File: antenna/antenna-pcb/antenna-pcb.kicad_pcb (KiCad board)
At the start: 2 copper layers, 97 x 97 mm, 11 parts, among them J1 SMA Connector Male, U1 HHM1589D1

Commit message: bottom adapter plate sanity commit
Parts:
- added Burn1: Burn, TestPoint:TestPoint_THTPad_2.0x2.0mm_Drill1.0mm, F.Cu at (146.0, 95.0)
- added Burn2: Burn, TestPoint:TestPoint_THTPad_2.0x2.0mm_Drill1.0mm, F.Cu at (142.0, 95.0)
- added Burn3: Burn, TestPoint:TestPoint_THTPad_2.0x2.0mm_Drill1.0mm, F.Cu at (150.0, 95.0)
- added Burn4: Burn, TestPoint:TestPoint_THTPad_2.0x2.0mm_Drill1.0mm, F.Cu at (154.0, 95.0)
- added GND1: GND, TestPoint:TestPoint_THTPad_2.0x2.0mm_Drill1.0mm, F.Cu at (150.0, 100.0)
- added GND2: GND, TestPoint:TestPoint_THTPad_2.0x2.0mm_Drill1.0mm, F.Cu at (146.0, 100.0)
- added GND3: GND, TestPoint:TestPoint_THTPad_2.0x2.0mm_Drill1.0mm, F.Cu at (154.0, 100.0)
- added GND4: GND, TestPoint:TestPoint_THTPad_2.0x2.0mm_Drill1.0mm, F.Cu at (142.0, 100.0)

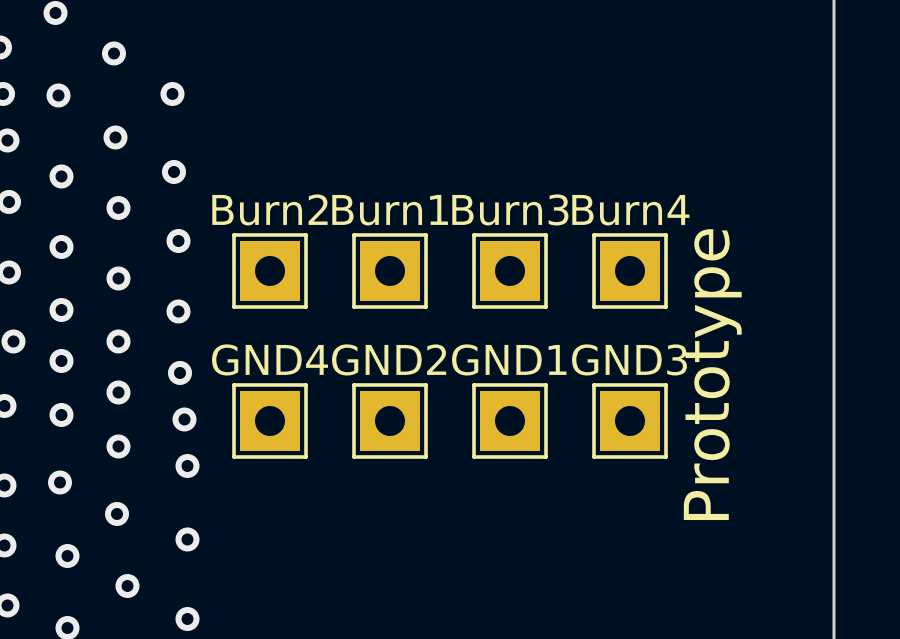
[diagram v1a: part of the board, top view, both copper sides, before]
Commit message: placed components, added traces to antenna-solar
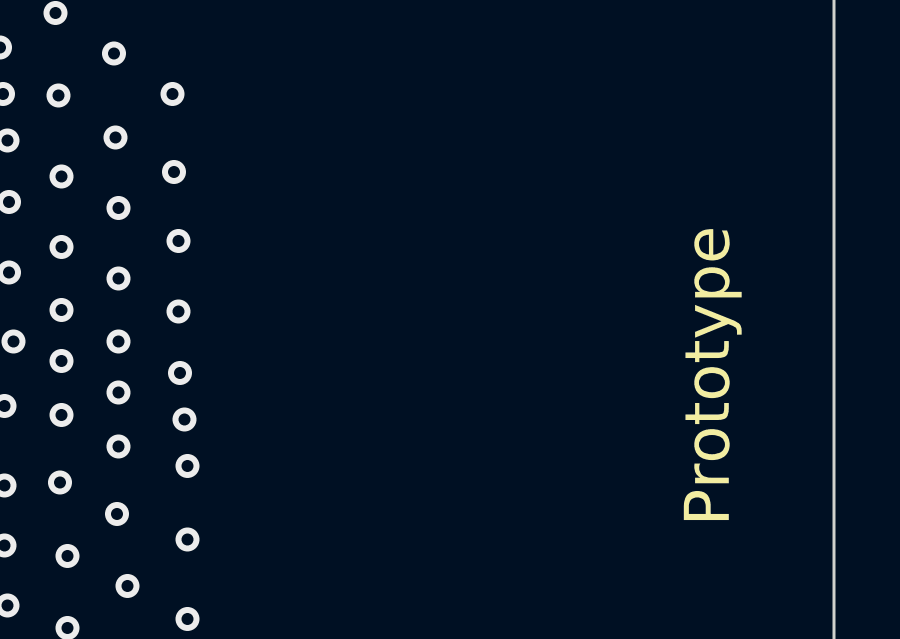
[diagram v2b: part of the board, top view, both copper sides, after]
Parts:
- removed Burn1, Burn2, Burn3, Burn4: Burn, TestPoint:TestPoint_THTPad_2.0x2.0mm_Drill1.0mm
- removed GND1, GND2, GND3, GND4: GND, TestPoint:TestPoint_THTPad_2.0x2.0mm_Drill1.0mm

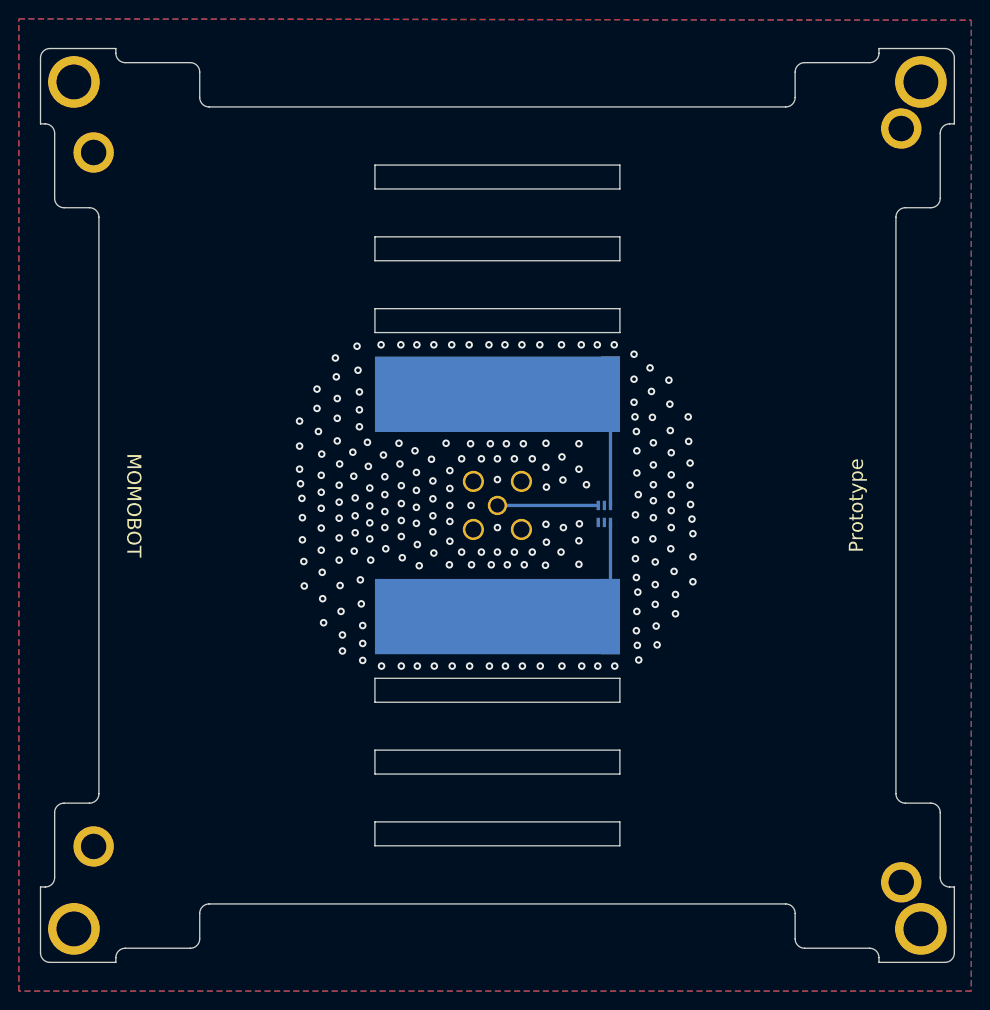
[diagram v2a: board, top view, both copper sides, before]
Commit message: updated antenna pcb
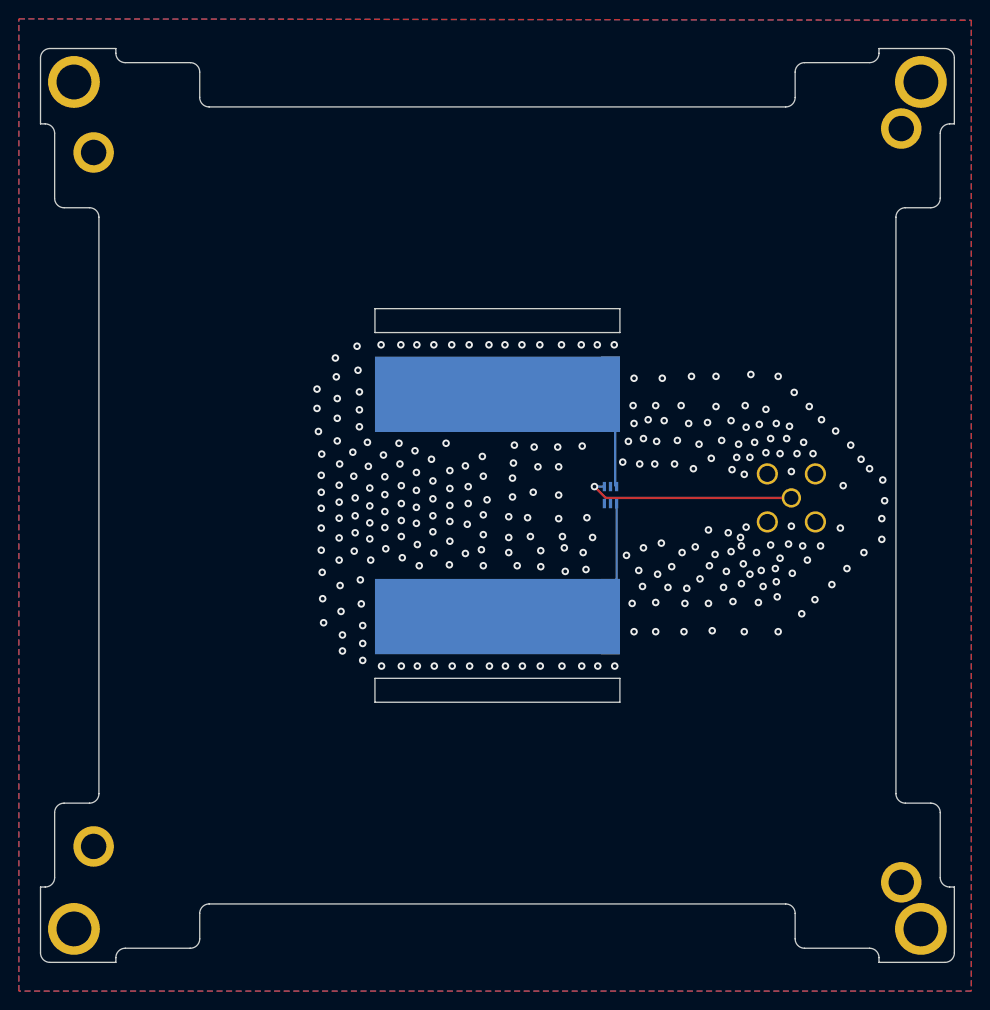
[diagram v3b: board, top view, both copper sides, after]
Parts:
- moved J1 31.2 mm to (149.7, 97.7)
- moved U1 2.10 mm to (130.5, 97.4)
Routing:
- net Net-(J1-Pad1): track 10.7 -> 22.4 mm, vias 0 -> 1
- net Net-(AE1-Pad2): track 10.0 -> 12.3 mm
- net Net-(AE1-Pad1): track 11.8 -> 10.1 mm
- net GND: vias 209 -> 267
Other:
- outline, holes or cut-outs redrawn
- board text removed: "MOMOBOT"
- board text removed: "Prototype"

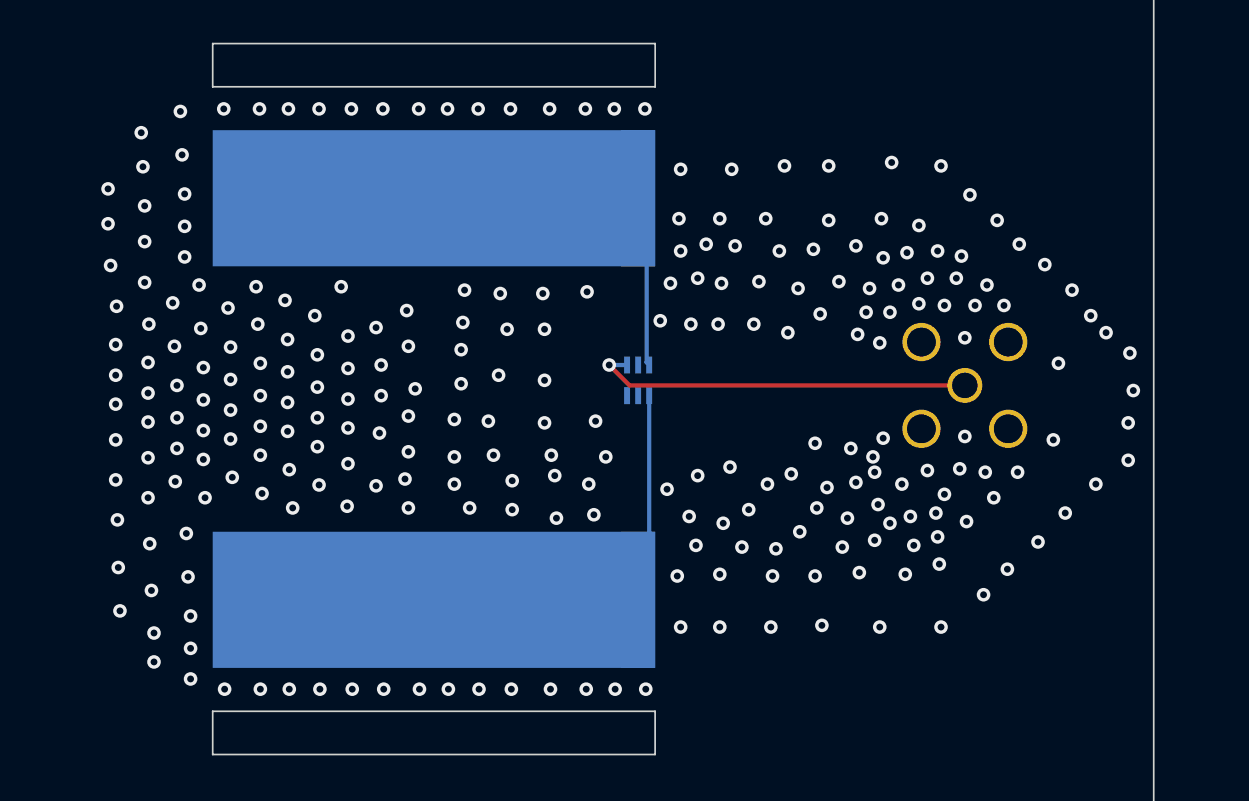
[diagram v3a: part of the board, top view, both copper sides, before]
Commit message: fixed balun placement and wiring
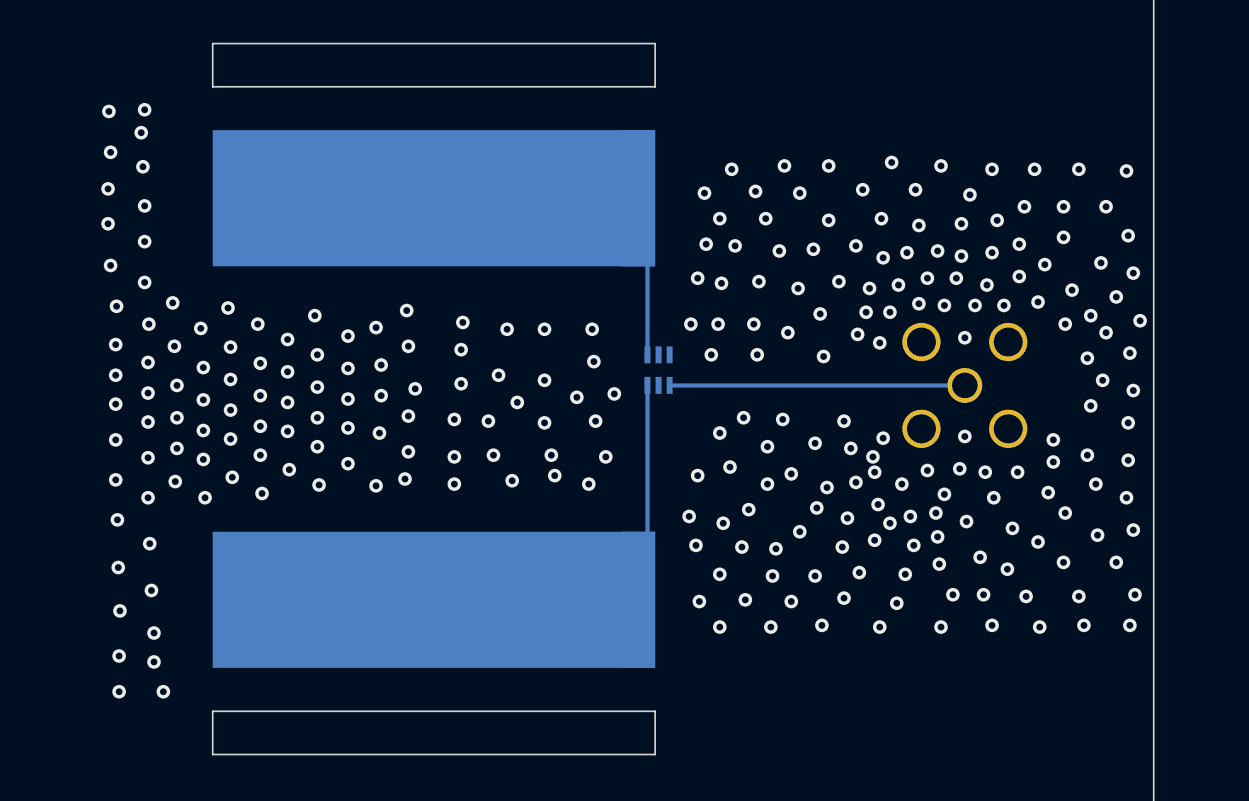
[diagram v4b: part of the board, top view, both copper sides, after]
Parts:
- moved U1 1.34 mm to (131.7, 96.8), turned to 90 degrees
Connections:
- AE1 pad 1: Net-(AE1-Pad1) -> Net-(U1-Pad4)
- AE1 pad 2: Net-(AE1-Pad2) -> Net-(U1-Pad3)
- U1 pad 3: Net-(AE1-Pad1) -> Net-(U1-Pad3)
- U1 pad 4: Net-(AE1-Pad2) -> Net-(U1-Pad4)
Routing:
- net Net-(U1-Pad3): track 0.00 -> 13.7 mm
- net Net-(AE1-Pad2): track 12.3 -> 0.00 mm
- net Net-(AE1-Pad1): track 10.1 -> 0.00 mm
- net Net-(U1-Pad4): track 0.00 -> 9.43 mm
- net Net-(J1-Pad1): track 22.4 -> 17.3 mm, vias 1 -> 0
- net GND: vias 267 -> 273
